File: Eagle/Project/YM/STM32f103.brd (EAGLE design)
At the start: 174.2 x 88.8 mm, 78 parts, among them IC1 YM3812, IC10 YM3812, IC11 YM3014B, IC12 LM358N, IC13 BA033CC0T, IC14 74ALS04N, IC15 6N136, IC2 YM3014B, IC3 LM358N, IC4 YM3812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

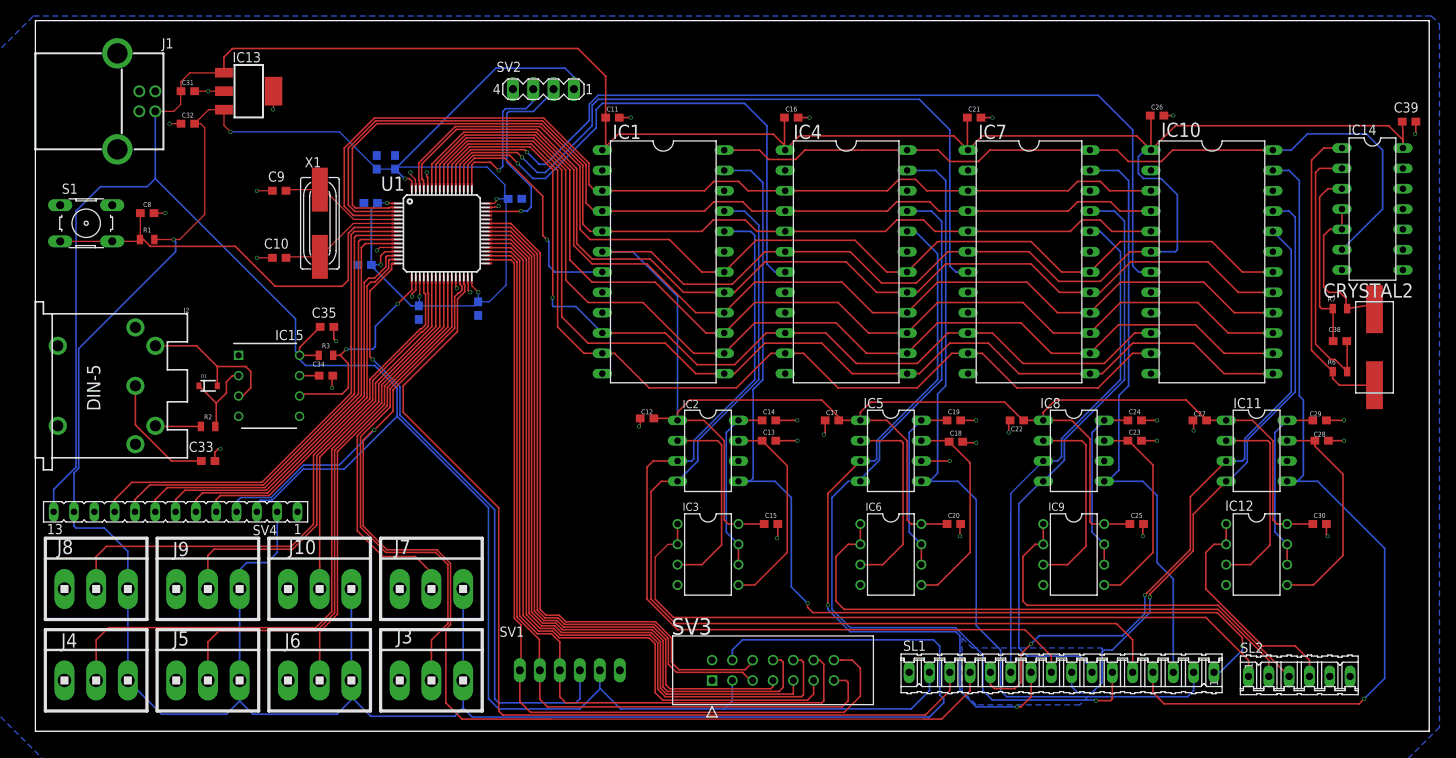
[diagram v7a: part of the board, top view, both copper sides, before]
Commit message: V4.0 ON/OFF Button/LED
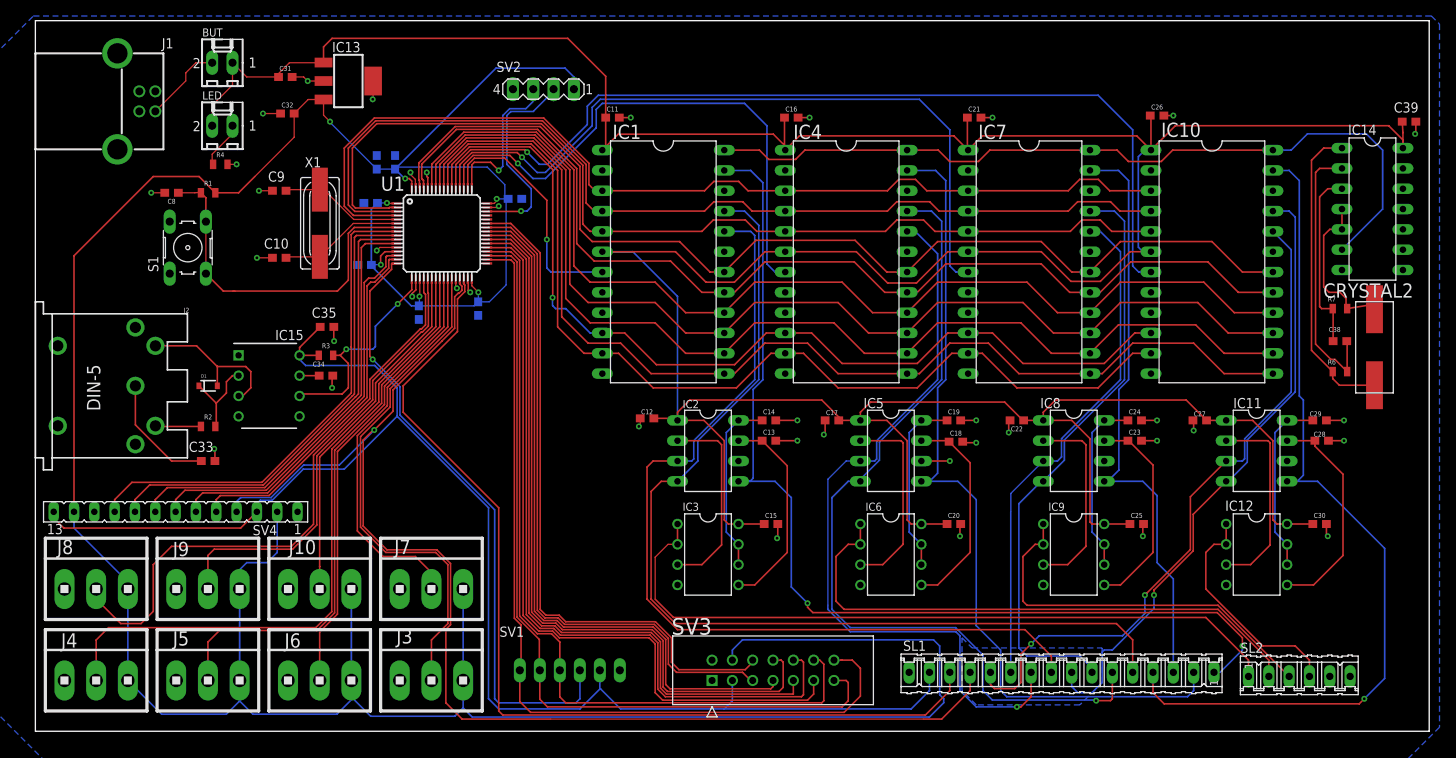
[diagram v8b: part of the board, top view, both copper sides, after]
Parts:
- added BUT, LED: 22-27-2021-02, con-molex:6410-02
- added R4: 1K, +HU-Lib:0805-SMD
- moved S1 13.1 mm to (19.1, 60.5), turned to 90 degrees
- moved C32 12.5 mm to (31.5, 77.2)
- moved IC13 12.5 mm to (39.1, 81.3)
- moved C31 12.3 mm to (31.2, 81.8)
- moved R1 9.60 mm to (21.6, 67.3)
- moved C8 3.97 mm to (17.0, 67.3), turned to 180 degrees
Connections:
- new net 5VBUTTON: BUT.2, J1.1
- new net N$13: LED.1, R4.1
- net 5V: now also BUT.1, LED.2; no longer J1.1
- net GND: now also R4.2
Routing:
- net 5V: track 733.6 -> 665.6 mm
- net 5VBUTTON: track 0.00 -> 10.2 mm
- net RST: track 54.3 -> 44.6 mm
- net N$13: track 0.00 -> 5.93 mm
- net ADC1: track 69.5 -> 74.9 mm
- net 3.3V: track 420.1 -> 417.2 mm, vias 8 -> 7
- net GND: track 71.9 -> 73.7 mm, vias 38 -> 39
- net YM-D4: track 135.4 -> 137.2 mm
- net YM-D5: track 134.1 -> 135.6 mm
- net YM-D3: track 136.9 -> 138.3 mm
- net YM2-SYNC: track 94.2 -> 95.2 mm, vias 2 -> 1
